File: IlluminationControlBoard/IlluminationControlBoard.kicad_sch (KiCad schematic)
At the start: 6 parts, among them J1 LIGHT1OUT, J2 12V_IN, J3 LIGHT2OUT, J4 PWM_SIGNALS

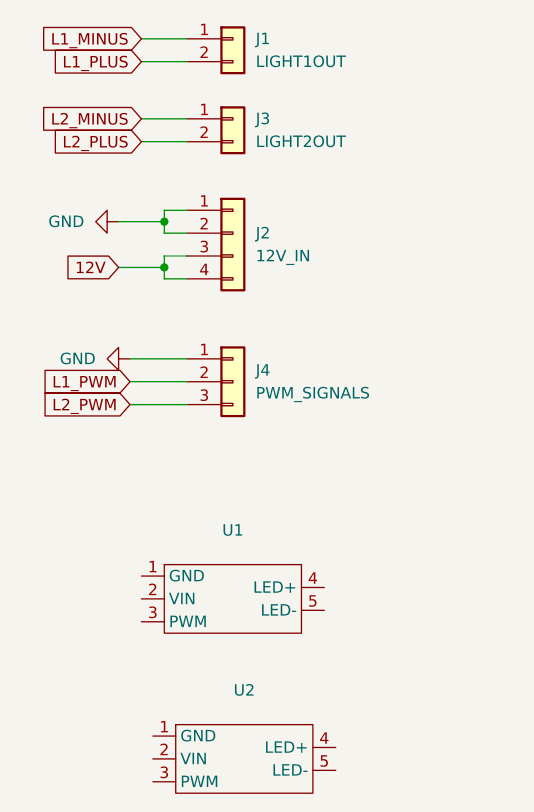
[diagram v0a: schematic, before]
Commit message: Schematic updates
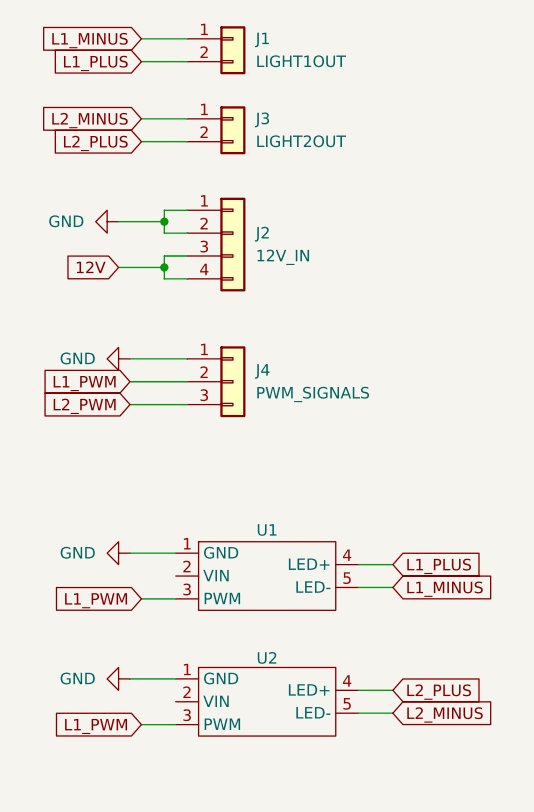
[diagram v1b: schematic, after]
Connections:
- net GND: now also U1.1 (GND), U2.1 (GND)
- net L1_MINUS: now also U1.5 (LED-)
- net L1_PLUS: now also U1.4 (LED+)
- net L1_PWM: now also U1.3 (PWM), U2.3 (PWM)
- net L2_MINUS: now also U2.5 (LED-)
- net L2_PLUS: now also U2.4 (LED+)
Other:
- moved on the sheet: U1, U2
